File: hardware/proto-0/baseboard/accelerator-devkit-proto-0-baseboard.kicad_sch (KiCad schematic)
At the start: 4 parts

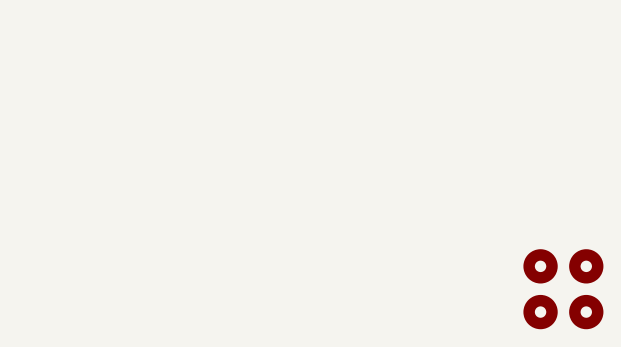
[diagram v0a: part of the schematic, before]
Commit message: Adding logo connections between schematic and PCB.
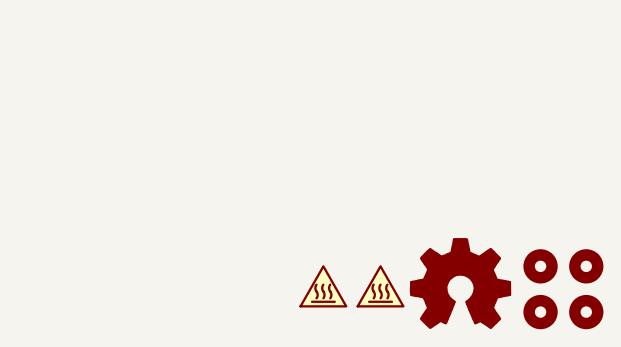
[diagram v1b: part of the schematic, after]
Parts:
- added LOGO1: Logo_Open_Hardware_Small, Symbol:OSHW-Symbol_6.7x6mm_Copper, symbol Graphic:Logo_Open_Hardware_Small
- added LOGO2, LOGO3: SYM_Hot_Small, Symbol:OSHW-Logo2_7.3x6mm_Copper, symbol Graphic:SYM_Hot_Small
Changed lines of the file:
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@@
+    )
+  )
+  (symbol (lib_id "Graphic:SYM_Hot_Small") (at 241.3 203.2 0) (unit 1)
+    (property "Reference" "LOGO2" (id 0) (at 241.3 199.644 0)
+      (effects (font (size 1.27 1.27)) hide)
+    )
+    (property "Value" "SYM_Hot_Small" (id 1) (at 241.3 206.375 0)
+      (effects (font (size 1.27 1.27)) hide)
+    )
+    (property "Footprint" "Symbol:OSHW-Logo2_7.3x6mm_Copper" (id 2) (at 241.3 207.645 0)
+      (effects (font (size 1.27 1.27)) hide)
+    )
+    (property "Datasheet" "~" (id 3) (at 242.062 208.28 0)
+      (effects (font (size 1.27 1.27)) hide)
+    )
+  )
+  (symbol (lib_id "Graphic:SYM_Hot_Small") (at 247.65 203.2 0) (unit 1)
+    (property "Reference" "LOGO3" (id 0) (at 247.65 199.644 0)
+      (effects (font (size 1.27 1.27)) hide)
+    )
+    (property "Value" "SYM_Hot_Small" (id 1) (at 247.65 206.375 0)
+      (effects (font (size 1.27 1.27)) hide)
+    )
+    (property "Footprint" "Symbol:OSHW-Logo2_7.3x6mm_Copper" (id 2) (at 247.65 207.645 0)
+      (effects (font (size 1.27 1.27)) hide)
+    )
+    (property "Datasheet" "~" (id 3) (at 248.412 208.28 0)
+      (effects (font (size 1.27 1.27)) hide)
+    )
+  )
+  (symbol (lib_id "Graphic:Logo_Open_Hardware_Small") (at 256.54 203.2 0) (unit 1)
+    (property "Reference" "LOGO1" (id 0) (at 256.54 196.215 0)
+      (effects (font (size 1.27 1.27)) hide)
+    )
+    (property "Value" "Logo_Open_Hardware_Small" (id 1) (at 256.54 208.915 0)
+      (effects (font (size 1.27 1.27)) hide)
+    )
+    (property "Footprint" "Symbol:OSHW-Symbol_6.7x6mm_Copper" (id 2) (at 256.54 203.2 0)
+      (effects (font (size 1.27 1.27)) hide)
+    )
+    (property "Datasheet" "~" (id 3) (at 256.54 203.2 0)
+      (effects (font (size 1.27 1.27)) hide)
     )
   )
@@
       (reference "H4") (unit 1)
     )
+    (path "/17637c26-a728-4dcb-b9f7-10dbd3725317"
+      (reference "LOGO1") (unit 1)
+    )
+    (path "/247cfc8a-770d-4a15-aeea-7516d0384ca0"
+      (reference "LOGO2") (unit 1)
+    )
+    (path "/9c363db2-d1fa-4aed-bdf7-99947582941c"
+      (reference "LOGO3") (unit 1)
+    )
     (path "/cff1d039-7316-4f26-bee2-2abf5e357325/02ab9e13-9aa6-4a8c-9f9a-c54538ee85b4"
